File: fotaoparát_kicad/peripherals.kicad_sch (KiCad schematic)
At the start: 5 parts, among them J13 Micro_SD_Card_Det2

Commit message: mirne korekce
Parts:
- added C29: 100nF, Capacitor_SMD:C_0201_0603Metric, symbol Device:C
- added C30: 10uF, Capacitor_SMD:C_0201_0603Metric, symbol Device:C
- C3: value 4,7uF -> 10uF
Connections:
- net CAM_SCL is gone; now on net I2C_SCL: CAM_IN1.13 (Pin_13)
- net CAM_SDA is gone; now on net I2C_SDA: CAM_IN1.14 (Pin_14)
- net +3V3: now also C29.1, C30.1
- net GND: now also C29.2, C30.2

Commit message: Pridani konektoru pro tlacitka na schema
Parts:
- added C53, C54, C55, C56, C57, C58, C60, C61, C62: 100nF, Capacitor_SMD:C_0201_0603Metric, symbol Device:C
- added J2: BUTTONS, Connector_FFC-FPC:Hirose_FH12-12S-0.5SH_1x12-1MP_P0.50mm_Horizontal, symbol Connector:Conn_01x12_Pin
- added R15, R16, R17, R18, R19, R20, R21, R22, R23, R8: 10k, Resistor_SMD:R_0603_1608Metric, symbol Device:R
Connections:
- net +3V3: now also R15.1, R16.1, R17.1, R18.1, R19.1, R20.1, R21.1, R22.1, R23.1
- net GND: now also C53.2, C54.2, C55.2, C56.2, C57.2, C58.2, C60.2, C61.2, C62.2, J2.1 (Pin_1), J2.12 (Pin_12)
- new net: J2.2 (Pin_2), R8.2
- new net BUTT_1: C62.1, J2.3 (Pin_3), R23.2
- new net BUTT_2: C61.1, J2.4 (Pin_4), R22.2
- new net BUTT_3: C60.1, J2.5 (Pin_5), R21.2
- new net BUTT_4: C53.1, J2.6 (Pin_6), R20.2
- new net BUTT_5: C58.1, J2.7 (Pin_7), R19.2
- new net BUTT_6: C57.1, J2.8 (Pin_8), R18.2
- new net BUTT_7: C56.1, J2.9 (Pin_9), R17.2
- new net BUTT_8: C55.1, J2.10 (Pin_10), R16.2
- new net BUTT_9: C54.1, J2.11 (Pin_11), R15.2
- new net LED_A: R8.1

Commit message: Pridani asi poloviny lscs cisel
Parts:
- C29, C4, C53, C54, C55, C56, C57, C58, C60, C61, C62: LSCS Number (none) -> C668346
- C3, C30: LSCS Number (none) -> C962136
- CAM_IN1, DISPLAY_IN1: LSCS Number (none) -> C6250813
- J13: LSCS Number (none) -> C597972
- R8: value 10k -> 330R
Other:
- moved on the sheet: R8
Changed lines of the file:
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@@
 	(wire
 		(pts
+			(xy 172.72 60.96) (xy 160.02 60.96)
+		)
+		(stroke
+			(width 0)
+			(type default)
+		)
+	)
+	(wire
+		(pts
 			(xy 99.06 66.04) (xy 127 66.04)
 		)
@@
 	(wire
 		(pts
-			(xy 167.64 60.96) (xy 255.27 60.96)
+			(xy 180.34 60.96) (xy 255.27 60.96)
 		)
 		(stroke
@@
 			)
 		)
+		(property "LSCS Number" "C962136"
+			(at 50.8 26.67 90)
+			(effects
+				(font
+					(size 1.27 1.27)
+				)
+				(hide yes)
+			)
+		)
 		(pin "1"
 		)
@@
 			)
 		)
+		(property "LSCS Number" "C668346"
+			(at 222.25 77.47 0)
+			(effects
+				(font
+					(size 1.27 1.27)
+				)
+				(hide yes)
+			)
+		)
 		(pin "2"
 		)
@@
 			)
 		)
+		(property "LSCS Number" "C668346"
+			(at 184.15 77.47 0)
+			(effects
+				(font
+					(size 1.27 1.27)
+				)
+				(hide yes)
+			)
+		)
 		(pin "2"
 		)
@@
 			)
 		)
+		(property "LSCS Number" "C668346"
+			(at 191.77 77.47 0)
+			(effects
+				(font
+					(size 1.27 1.27)
+				)
+				(hide yes)
+			)
+		)
 		(pin "2"
 		)
@@
 			)
 		)
+		(property "LSCS Number" "C962136"
+			(at 130.81 25.4 90)
+			(effects
+				(font
+					(size 1.27 1.27)
+				)
+				(hide yes)
+			)
+		)
 		(pin "1"
 		)
@@
 			)
 		)
+		(property "LSCS Number" "C668346"
+			(at 237.49 77.47 0)
+			(effects
+				(font
+					(size 1.27 1.27)
+				)
+				(hide yes)
+			)
+		)
 		(pin "2"
 		)
@@
 			)
 		)
+		(property "LSCS Number" "C668346"
+			(at 199.39 77.47 0)
+			(effects
+				(font
+					(size 1.27 1.27)
+				)
+				(hide yes)
+			)
+		)
 		(pin "2"
 		)
@@
 			)
 		)
+		(property "LSCS Number" "C6250813"
+			(at 132.08 53.34 0)
+			(effects
+				(font
+					(size 1.27 1.27)
+				)
+				(hide yes)
+			)
+		)
 		(pin "3"
 		)
@@
 			)
 		)
+		(property "LSCS Number" "C668346"
+			(at 130.81 20.32 90)
+			(effects
+				(font
+					(size 1.27 1.27)
+				)
+				(hide yes)
+			)
+		)
 		(pin "1"
 		)
@@
 			)
 		)
+		(property "LSCS Number" "C6250813"
+			(at 35.56 45.72 0)
+			(effects
+				(font
+					(size 1.27 1.27)
+				)
+				(hide yes)
+			)
+		)
 		(pin "8"
 		)
@@
 			)
 		)
+		(property "LSCS Number" "C668346"
+			(at 229.87 77.47 0)
+			(effects
+				(font
+					(size 1.27 1.27)
+				)
+				(hide yes)
+			)
+		)
 		(pin "2"
 		)
@@
 			)
 		)
+		(property "LSCS Number" "C597972"
+			(at 52.07 132.08 0)
+			(effects
+				(font
+					(size 1.27 1.27)
+				)
+				(hide yes)
+			)
+		)
 		(pin "3"
 		)
@@
 			)
 		)
+		(property "LSCS Number" "C668346"
+			(at 207.01 77.47 0)
+			(effects
+				(font
+					(size 1.27 1.27)
+				)
+				(hide yes)
+			)
+		)
 		(pin "2"
 		)
@@
 			)
 		)
+		(property "LSCS Number" "C668346"
+			(at 214.63 77.47 0)
+			(effects
+				(font
+					(size 1.27 1.27)
+				)
+				(hide yes)
+			)
+		)
 		(pin "2"
 		)
@@
 			)
 		)
+		(property "LSCS Number" "C668346"
+			(at 245.11 77.47 0)
+			(effects
+				(font
+					(size 1.27 1.27)
+				)
+				(hide yes)
+			)
+		)
 		(pin "2"
 		)
@@
 			)
 		)
+		(property "LSCS Number" "C668346"
+			(at 50.8 21.59 90)
+			(effects
+				(font
+					(size 1.27 1.27)
+				)
+				(hide yes)
+			)
+		)
 		(pin "1"
 		)
@@
 	(symbol
 		(lib_id "Device:R")
-		(at 163.83 60.96 90)
+		(at 176.53 60.96 90)
 		(unit 1)
 		(exclude_from_sim no)
@@
 		(dnp no)
 		(property "Reference" "R8"
-			(at 165.1 63.5 90)
+			(at 177.8 63.5 90)
 			(effects
 				(font
@@
 			)
 		)
-		(property "Value" "10k"
-			(at 165.862 65.024 90)
+		(property "Value" "330R"
+			(at 178.562 65.024 90)
 			(effects
 				(font
@@
 		)
 		(property "Footprint" "Resistor_SMD:R_0603_1608Metric"
-			(at 163.83 62.738 90)
+			(at 176.53 62.738 90)
 			(effects
 				(font
@@
 		)
 		(property "Datasheet" "~"
-			(at 163.83 60.96 0)
+			(at 176.53 60.96 0)
 			(effects
 				(font
@@
 		)
 		(property "Description" "Resistor"
-			(at 163.83 60.96 0)
+			(at 176.53 60.96 0)
 			(effects
 				(font

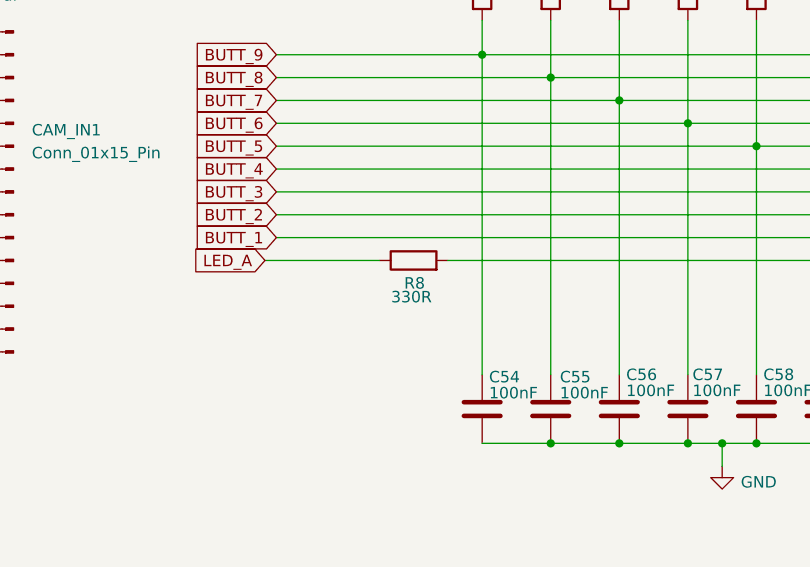
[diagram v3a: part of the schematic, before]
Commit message: PRidani (skoro) vsech lscs cisel, krystal je spatne ale pcb mam doma udelane jeste jinak, takze pridam a preroutuju pozdeji.
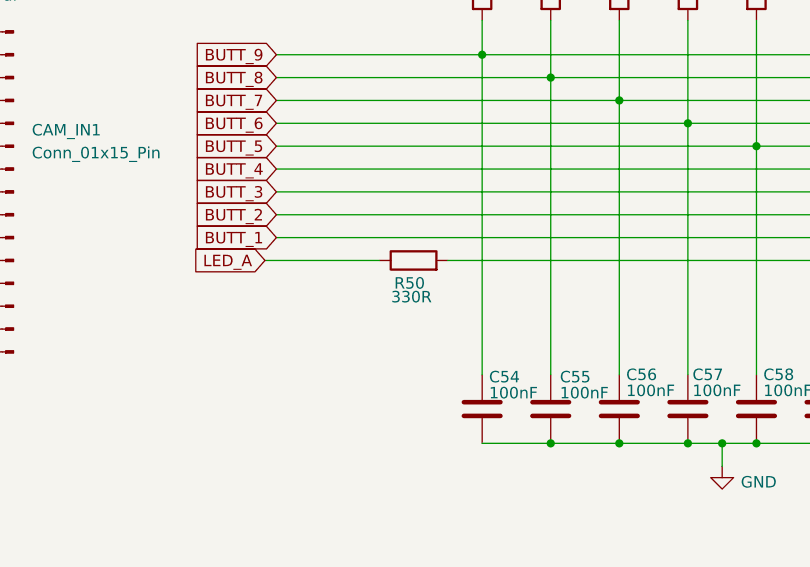
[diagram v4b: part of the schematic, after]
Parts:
- J2: LSCS Number (none) -> C88360
- R15, R16, R17, R18, R19, R20, R21, R22, R23: LSCS Number (none) -> C98220
- R50: renamed from R8; LSCS Number (none) -> C105881
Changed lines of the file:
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@@
+			)
+		)
+		(property "LSCS Number" "C98220"
+			(at 222.25 30.48 0)
+			(effects
+				(font
+					(size 1.27 1.27)
+				)
+				(hide yes)
 			)
 		)
@@
 		(on_board yes)
 		(dnp no)
-		(property "Reference" "#PWR0101"
+		(property "Reference" "#PWR0103"
 			(at 210.82 29.21 0)
 			(effects
@@
 			(project "fotaoparát"
 				(path "/0ab33720-0b6a-449c-80c0-2b7abe4d9450/be787f52-1025-4e17-92bf-51f58d5e4e6f"
-					(reference "#PWR0101")
+					(reference "#PWR0103")
 					(unit 1)
 				)
@@
 			)
 		)
+		(property "LSCS Number" "C98220"
+			(at 229.87 30.48 0)
+			(effects
+				(font
+					(size 1.27 1.27)
+				)
+				(hide yes)
+			)
+		)
 		(pin "1"
 		)
@@
 			)
 		)
+		(property "LSCS Number" "C98220"
+			(at 207.01 30.48 0)
+			(effects
+				(font
+					(size 1.27 1.27)
+				)
+				(hide yes)
+			)
+		)
 		(pin "1"
 		)
@@
 			)
 		)
+		(property "LSCS Number" "C98220"
+			(at 191.77 30.48 0)
+			(effects
+				(font
+					(size 1.27 1.27)
+				)
+				(hide yes)
+			)
+		)
 		(pin "1"
 		)
@@
 		)
 		(property "Description" "Resistor"
+			(at 199.39 30.48 0)
+			(effects
+				(font
+					(size 1.27 1.27)
+				)
+				(hide yes)
+			)
+		)
+		(property "LSCS Number" "C98220"
 			(at 199.39 30.48 0)
 			(effects
@@
 			)
 		)
+		(property "LSCS Number" "C98220"
+			(at 237.49 30.48 0)
+			(effects
+				(font
+					(size 1.27 1.27)
+				)
+				(hide yes)
+			)
+		)
 		(pin "1"
 		)
@@
 			)
 		)
+		(property "LSCS Number" "C98220"
+			(at 184.15 30.48 0)
+			(effects
+				(font
+					(size 1.27 1.27)
+				)
+				(hide yes)
+			)
+		)
 		(pin "1"
 		)
@@
 			)
 		)
+		(property "LSCS Number" "C88360"
+			(at 260.35 50.8 0)
+			(effects
+				(font
+					(size 1.27 1.27)
+				)
+				(hide yes)
+			)
+		)
 		(pin "11"
 		)
@@
 		)
 		(property "Description" "Resistor"
+			(at 245.11 30.48 0)
+			(effects
+				(font
+					(size 1.27 1.27)
+				)
+				(hide yes)
+			)
+		)
+		(property "LSCS Number" "C98220"
 			(at 245.11 30.48 0)
 			(effects
@@
 		(on_board yes)
 		(dnp no)
-		(property "Reference" "#PWR0102"
+		(property "Reference" "#PWR0104"
 			(at 210.82 90.17 0)
 			(effects
@@
 			(project "fotaoparát"
 				(path "/0ab33720-0b6a-449c-80c0-2b7abe4d9450/be787f52-1025-4e17-92bf-51f58d5e4e6f"
-					(reference "#PWR0102")
+					(reference "#PWR0104")
 					(unit 1)
 				)
@@
 			)
 		)
+		(property "LSCS Number" "C98220"
+			(at 214.63 30.48 0)
+			(effects
+				(font
+					(size 1.27 1.27)
+				)
+				(hide yes)
+			)
+		)
 		(pin "1"
 		)
@@
 		(on_board yes)
 		(dnp no)
-		(property "Reference" "R8"
+		(property "Reference" "R50"
 			(at 177.8 63.5 90)
 			(effects
@@
 			)
 		)
+		(property "LSCS Number" "C105881"
+			(at 176.53 60.96 90)
+			(effects
+				(font
+					(size 1.27 1.27)
+				)
+				(hide yes)
+			)
+		)
 		(pin "1"
 		)
@@
 			(project "fotaoparát"
 				(path "/0ab33720-0b6a-449c-80c0-2b7abe4d9450/be787f52-1025-4e17-92bf-51f58d5e4e6f"
-					(reference "R8")
-					(unit 1)
-				)
+					(reference "R50")
+					(unit 1)
+				)
